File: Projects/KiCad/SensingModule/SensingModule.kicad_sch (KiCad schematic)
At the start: 37 parts, among them J3 Micro_SD_Card_Det_Hirose_DM3AT, J4 Conn_01x02_Pin, J5 Conn_01x05_Socket, J7 Conn_01x05_Pin, Q1 DTC143E, U1 NUCLEO-F303K8, U10 24LC1025, U11 MB85RS2MT, U12 TLP222A, U2 MCP2562-E-P, U3 24LC1025, U5 LT1584-3.3, U7 24LC1025, U8 MB85RS2MT, U9 24LC1025

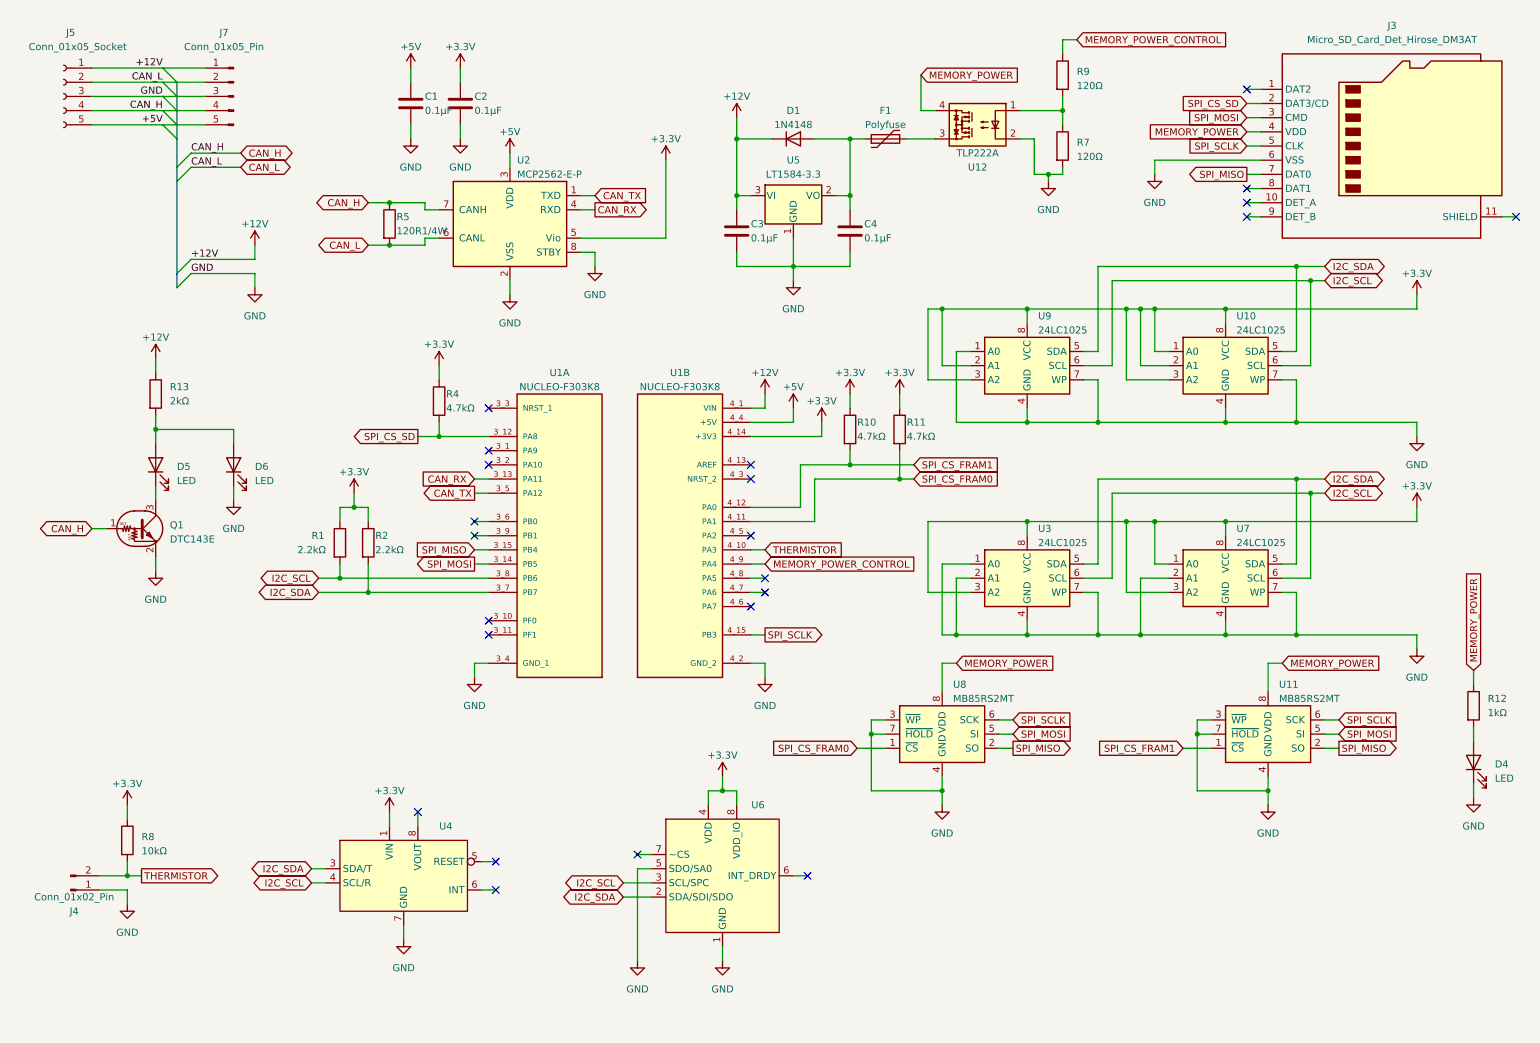
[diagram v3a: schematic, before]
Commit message: RCを解決
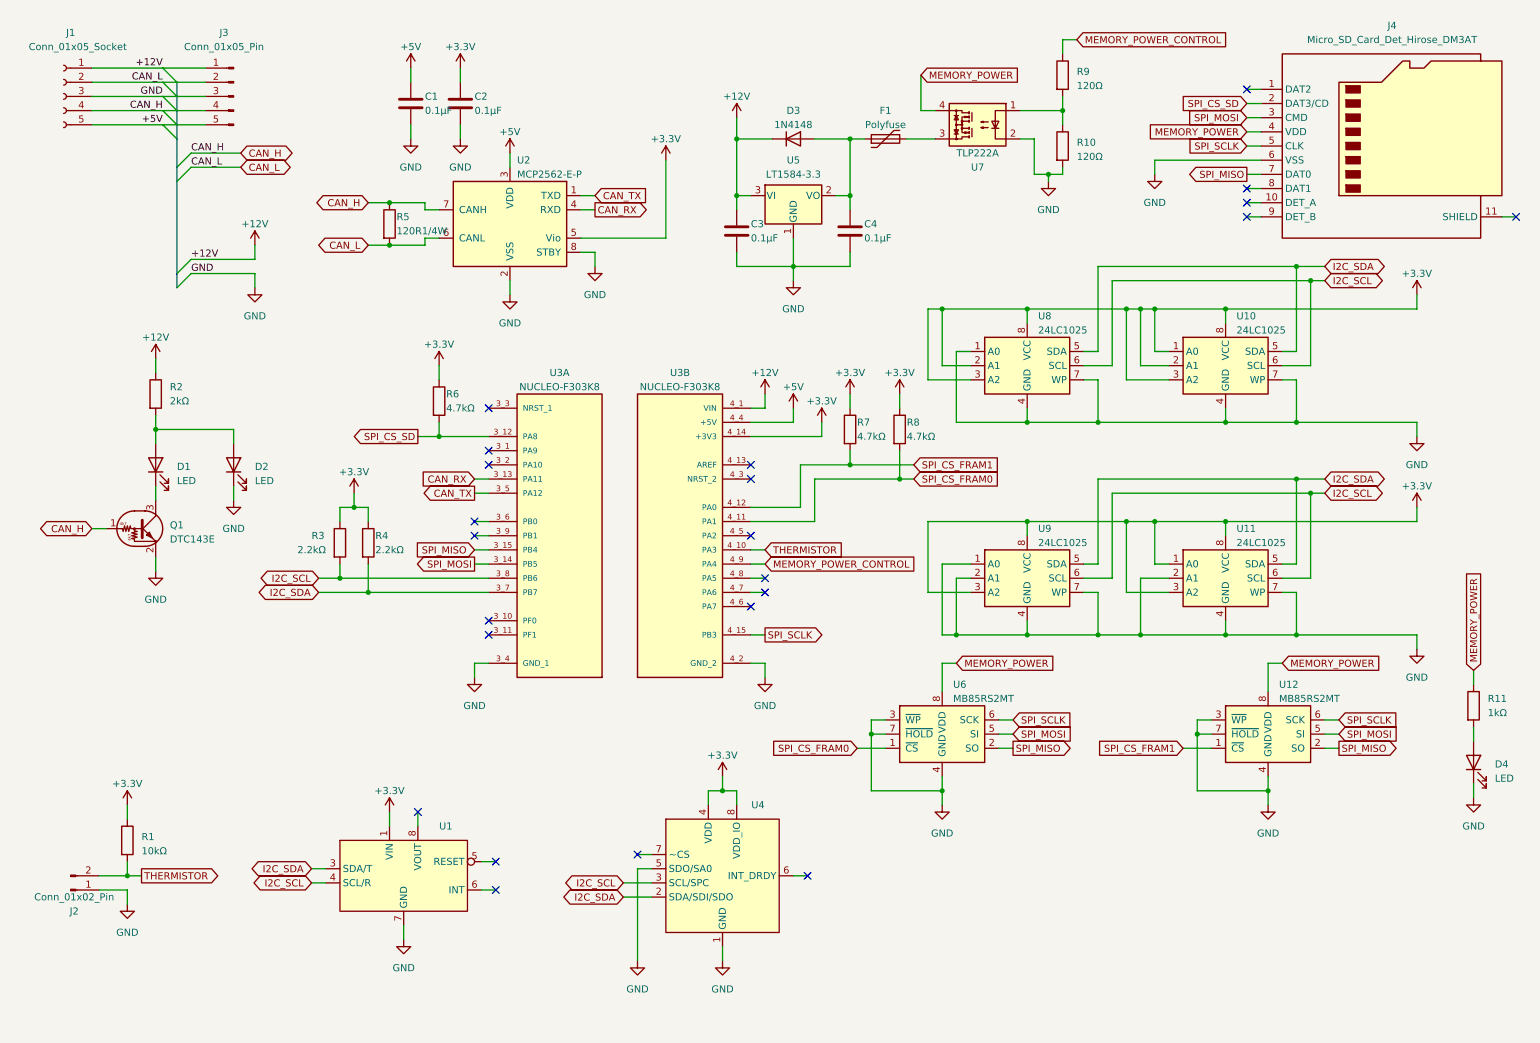
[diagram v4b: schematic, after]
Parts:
- renumbered D5 to D1, D6 to D2, D1 to D3, J5 to J1, J4 to J2, J7 to J3, J3 to J4, R8 to R1, R7 to R10, R12 to R11, R13 to R2, R1 to R3, R2 to R4, R4 to R6, R10 to R7, R11 to R8, U4 to U1, U7 to U11, U11 to U12, U1 to U3, U6 to U4, U8 to U6, U12 to U7, U9 to U8, U3 to U9

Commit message: 計測モジュールの基板設計概ね終わり
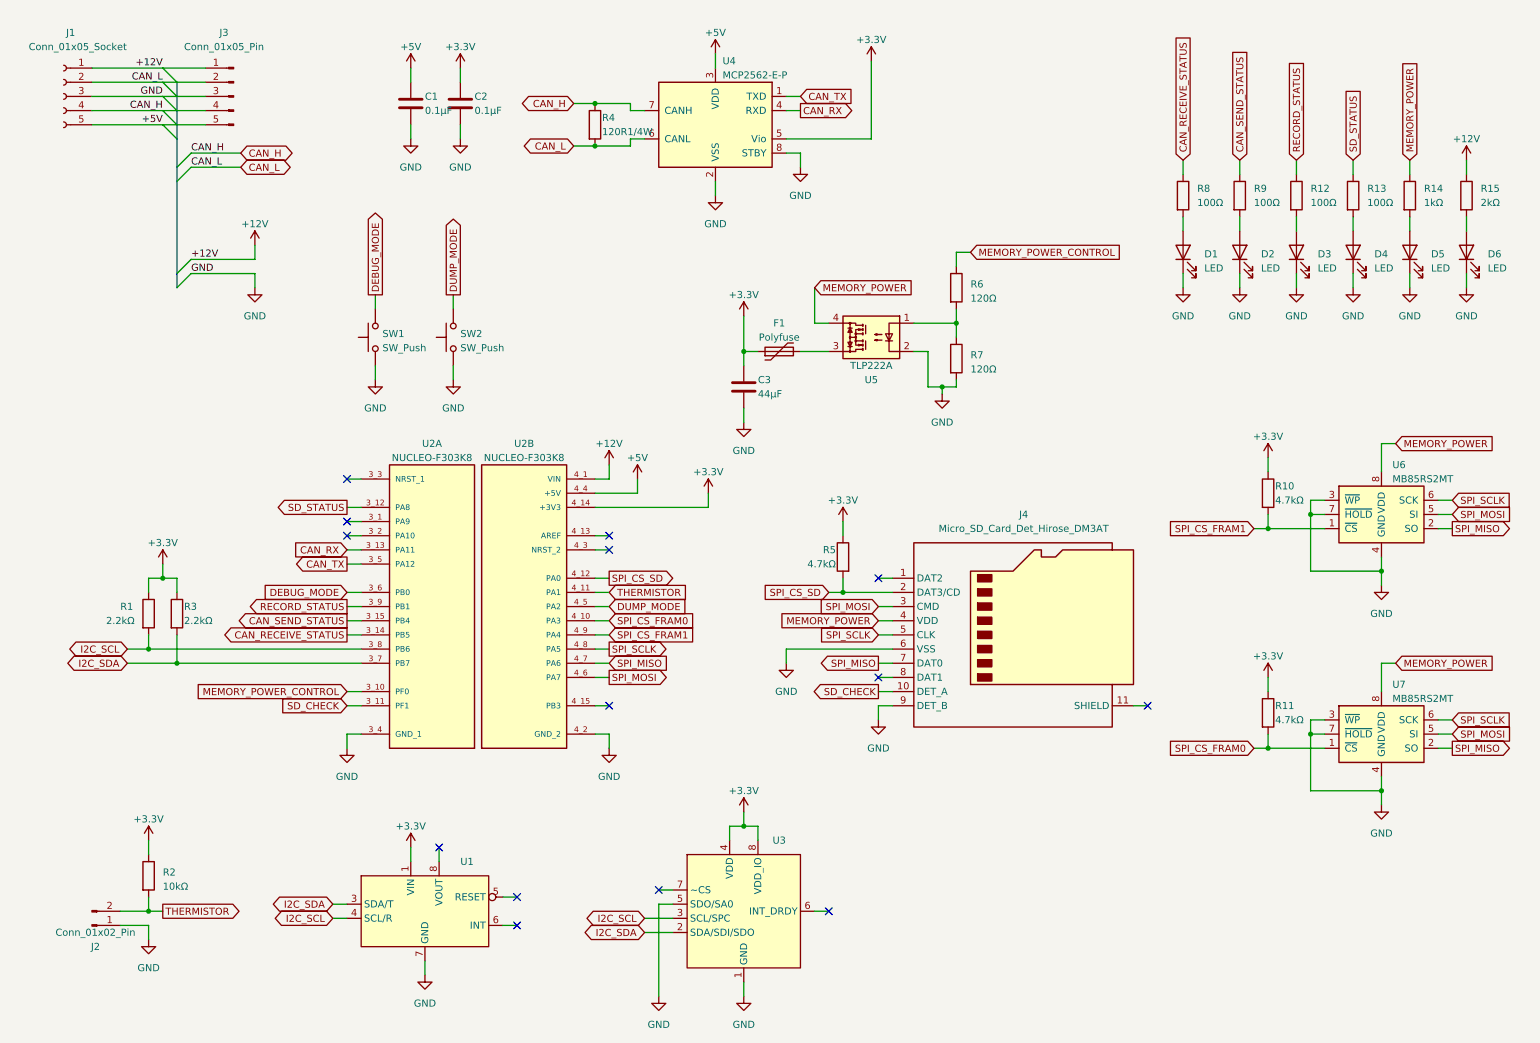
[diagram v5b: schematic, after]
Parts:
- removed C4: 0.1μF, Capacitor_SMD:C_0805_2012Metric_Pad1.18x1.45mm_HandSolder, symbol Device:C
- removed D3: 1N4148, Diode_THT:D_DO-35_SOD27_P7.62mm_Horizontal, symbol Diode:1N4148
- removed Q1: DTC143E, Package_TO_SOT_THT:TO-92_Inline, symbol Transistor_BJT:DTC143E
- removed U10, U11, U8, U9: 24LC1025, Package_DIP:DIP-8_W7.62mm, symbol Memory_EEPROM:24LC1025
- removed U5: LT1584-3.3, Package_TO_SOT_THT:TO-220-3_Vertical, symbol Regulator_Linear:LT1584-3.3
- added D2, D3, D4: LED, LED_SMD:LED_1206_3216Metric_Pad1.42x1.75mm_HandSolder, symbol Device:LED
- added R12, R13, R8, R9: 100Ω, Resistor_SMD:R_0805_2012Metric_Pad1.20x1.40mm_HandSolder, symbol Device:R
- added SW1, SW2: SW_Push, Button_Switch_THT:SW_PUSH_6mm, symbol Switch:SW_Push
- C3: value 0.1μF -> 44μF
- renumbered D4 to D5, D2 to D6, R3 to R1, R8 to R10, R7 to R11, R11 to R14, R2 to R15, R1 to R2, R4 to R3, R5 to R4, R6 to R5, R9 to R6, R10 to R7, U3 to U2, U4 to U3, U2 to U4, U7 to U5, U12 to U6, U6 to U7
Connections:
- net +12V: no longer C3.1
- net +3.3V: now also C3.1, F1.1
- net GND: now also D1.1 (K), J4.9 (DET_B), D2.1 (K), D3.1 (K), D4.1 (K), SW1.1, SW2.1
- net MEMORY_POWER_CONTROL: now also U2.3_10 (PF0); no longer U2.4_9 (PA4)
- net SPI_CS_FRAM0: now also R11.2, U2.4_10 (PA3); no longer R10.2, U2.4_11 (PA1)
- net SPI_CS_FRAM1: now also R10.2, U2.4_9 (PA4); no longer R11.2, U2.4_12 (PA0)
- net SPI_CS_SD: now also U2.4_12 (PA0); no longer U2.3_12 (PA8)
- net SPI_MISO: now also U2.4_7 (PA6); no longer U2.3_15 (PB4)
- net SPI_MOSI: now also U2.4_6 (PA7); no longer U2.3_14 (PB5)
- net SPI_SCLK: now also U2.4_8 (PA5); no longer U2.4_15 (PB3)
- net THERMISTOR: now also U2.4_11 (PA1); no longer U2.4_10 (PA3)
- net at D6.2 (A), R15.2: no longer D1.2 (A)
- net DUMP_MODE: now reaches U2.4_5 (PA2)
- net DUMP_MODE: now also SW2.2
- net SD_CHECK: now reaches J4.10 (DET_A)
- net SD_CHECK: now also U2.3_11 (PF1)
- net DEBUG_MODE: now reaches U2.3_6 (PB0)
- net DEBUG_MODE: now also SW1.2
- net RECORD_STATUS: now reaches U2.3_9 (PB1)
- net RECORD_STATUS: now also R12.1
- new net: D4.2 (A), R13.2
- new net: D2.2 (A), R9.2
- new net: D3.2 (A), R12.2
- new net: D1.2 (A), R8.2
- new net CAN_RECEIVE_STATUS: R8.1, U2.3_14 (PB5)
- new net CAN_SEND_STATUS: R9.1, U2.3_15 (PB4)
- new net SD_STATUS: R13.1, U2.3_12 (PA8)
- no-connect marks 23 -> 14
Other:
- moved on the sheet: D5, D6, F1, J2, J4, R1, R10, R11, R14, R15, R2, R3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

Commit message: 計測モジュールとフライトモジュール終わり
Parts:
- removed C3: 44μF, Capacitor_SMD:C_0805_2012Metric_Pad1.18x1.45mm_HandSolder, symbol Device:C
- removed U3: ~, StrawberryLinux_LPS33HW_Module:LPS33HW, symbol StrawberryLinux_LPS33HW_Module:LPS33HW
- added C3: 470μF, Capacitor_THT:CP_Radial_D10.0mm_P3.50mm, symbol Device:C_Polarized
- added U3: ~, Akizuki_BME280_Module:BME280, symbol Akizuki_BME280_Module:BME280
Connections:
- net +3.3V: now also C3.1, U3.1 (VDD), U3.3 (SCB)
- net GND: now also C3.2, U3.2 (GND), U3.5 (SDO)
- net I2C_SCL: now also U3.6 (SCK)
- net I2C_SDA: now also U3.4 (SDI)
- no-connect marks 14 -> 12

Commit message: アルミ殿下を導電性高分子アルミ固体電解コンデンサに変更
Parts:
- C3: value 470μF -> 100μF; footprint Capacitor_THT:CP_Radial_D10.0mm_P3.50mm -> Capacitor_SMD:CP_Elec_6.3x7.7
- R1, R3: value 2.2kΩ -> 10kΩ
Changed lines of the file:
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@@
       (effects (font (size 1.27 1.27)) (justify left))
     )
-    (property "Value" "2.2kΩ" (at 29.21 124.46 0)
+    (property "Value" "10kΩ" (at 29.21 124.46 0)
       (effects (font (size 1.27 1.27)) (justify left))
     )
@@
       (effects (font (size 1.27 1.27)) (justify left))
     )
-    (property "Value" "2.2kΩ" (at 43.18 124.46 0)
+    (property "Value" "10kΩ" (at 43.18 124.46 0)
       (effects (font (size 1.27 1.27)) (justify left))
     )
@@
       (effects (font (size 1.27 1.27)) (justify left))
     )
-    (property "Value" "470μF" (at 147.32 83.566 0)
-      (effects (font (size 1.27 1.27)) (justify left))
-    )
-    (property "Footprint" "Capacitor_THT:CP_Radial_D10.0mm_P3.50mm" (at 144.4752 86.36 0)
-      (effects (font (size 1.27 1.27)) hide)
-    )
+    (property "Value" "100μF" (at 147.32 83.566 0)
+      (effects (font (size 1.27 1.27)) (justify left))
+    )
+    (property "Footprint" "Capacitor_SMD:CP_Elec_6.3x7.7" (at 144.4752 86.36 0)
+      (effects (font (size 1.27 1.27)) hide)
+    )

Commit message: 抵抗とLEDを1608に変更
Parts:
- D1, D2, D3, D4, D5, D6: footprint LED_SMD:LED_1206_3216Metric_Pad1.42x1.75mm_HandSolder -> LED_SMD:LED_0603_1608Metric_Pad1.05x0.95mm_HandSolder
- R1, R10, R11, R12, R13, R14, R15, R2, R3, R4, R5, R6, R7, R8, R9: footprint Resistor_SMD:R_0805_2012Metric_Pad1.20x1.40mm_HandSolder -> Resistor_SMD:R_0603_1608Metric_Pad0.98x0.95mm_HandSolder
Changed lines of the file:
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@@
       (effects (font (size 1.27 1.27)) (justify left))
     )
-    (property "Footprint" "Resistor_SMD:R_0805_2012Metric_Pad1.20x1.40mm_HandSolder" (at 179.832 64.77 90)
+    (property "Footprint" "Resistor_SMD:R_0603_1608Metric_Pad0.98x0.95mm_HandSolder" (at 179.832 64.77 90)
       (effects (font (size 1.27 1.27)) hide)
     )
@@
       (effects (font (size 1.27 1.27)) (justify right))
     )
-    (property "Footprint" "LED_SMD:LED_1206_3216Metric_Pad1.42x1.75mm_HandSolder" (at 252.73 58.42 0)
+    (property "Footprint" "LED_SMD:LED_0603_1608Metric_Pad1.05x0.95mm_HandSolder" (at 252.73 58.42 0)
       (effects (font (size 1.27 1.27)) hide)
     )
@@
       (effects (font (size 1.27 1.27)) (justify left))
     )
-    (property "Footprint" "Resistor_SMD:R_0805_2012Metric_Pad1.20x1.40mm_HandSolder" (at 250.952 48.26 90)
+    (property "Footprint" "Resistor_SMD:R_0603_1608Metric_Pad0.98x0.95mm_HandSolder" (at 250.952 48.26 90)
       (effects (font (size 1.27 1.27)) hide)
     )
@@
       (effects (font (size 1.27 1.27)) (justify left))
     )
-    (property "Footprint" "Resistor_SMD:R_0805_2012Metric_Pad1.20x1.40mm_HandSolder" (at 230.632 48.26 90)
+    (property "Footprint" "Resistor_SMD:R_0603_1608Metric_Pad0.98x0.95mm_HandSolder" (at 230.632 48.26 90)
       (effects (font (size 1.27 1.27)) hide)
     )
@@
       (effects (font (size 1.27 1.27)) (justify left))
     )
-    (property "Footprint" "Resistor_SMD:R_0805_2012Metric_Pad1.20x1.40mm_HandSolder" (at 271.272 48.26 90)
+    (property "Footprint" "Resistor_SMD:R_0603_1608Metric_Pad0.98x0.95mm_HandSolder" (at 271.272 48.26 90)
       (effects (font (size 1.27 1.27)) hide)
     )
@@
       (effects (font (size 1.27 1.27)) (justify left))
     )
-    (property "Footprint" "Resistor_SMD:R_0805_2012Metric_Pad1.20x1.40mm_HandSolder" (at 35.052 170.18 90)
+    (property "Footprint" "Resistor_SMD:R_0603_1608Metric_Pad0.98x0.95mm_HandSolder" (at 35.052 170.18 90)
       (effects (font (size 1.27 1.27)) hide)
     )
@@
       (effects (font (size 1.27 1.27)) (justify right))
     )
-    (property "Footprint" "LED_SMD:LED_1206_3216Metric_Pad1.42x1.75mm_HandSolder" (at 242.57 58.42 0)
+    (property "Footprint" "LED_SMD:LED_0603_1608Metric_Pad1.05x0.95mm_HandSolder" (at 242.57 58.42 0)
       (effects (font (size 1.27 1.27)) hide)
     )
@@
       (effects (font (size 1.27 1.27)) (justify left))
     )
-    (property "Footprint" "Resistor_SMD:R_0805_2012Metric_Pad1.20x1.40mm_HandSolder" (at 163.068 113.03 90)
+    (property "Footprint" "Resistor_SMD:R_0603_1608Metric_Pad0.98x0.95mm_HandSolder" (at 163.068 113.03 90)
       (effects (font (size 1.27 1.27)) hide)
     )
@@
       (effects (font (size 1.27 1.27)) (justify left))
     )
-    (property "Footprint" "Resistor_SMD:R_0805_2012Metric_Pad1.20x1.40mm_HandSolder" (at 240.792 48.26 90)
+    (property "Footprint" "Resistor_SMD:R_0603_1608Metric_Pad0.98x0.95mm_HandSolder" (at 240.792 48.26 90)
       (effects (font (size 1.27 1.27)) hide)
     )
@@
       (effects (font (size 1.27 1.27)) (justify left))
     )
-    (property "Footprint" "Resistor_SMD:R_0805_2012Metric_Pad1.20x1.40mm_HandSolder" (at 261.112 48.26 90)
+    (property "Footprint" "Resistor_SMD:R_0603_1608Metric_Pad0.98x0.95mm_HandSolder" (at 261.112 48.26 90)
       (effects (font (size 1.27 1.27)) hide)
     )
@@
       (effects (font (size 1.27 1.27)) (justify left))
     )
-    (property "Footprint" "Resistor_SMD:R_0805_2012Metric_Pad1.20x1.40mm_HandSolder" (at 235.712 140.97 90)
+    (property "Footprint" "Resistor_SMD:R_0603_1608Metric_Pad0.98x0.95mm_HandSolder" (at 235.712 140.97 90)
       (effects (font (size 1.27 1.27)) hide)
     )
@@
       (effects (font (size 1.27 1.27)) (justify left))
     )
-    (property "Footprint" "Resistor_SMD:R_0805_2012Metric_Pad1.20x1.40mm_HandSolder" (at 35.052 123.19 90)
+    (property "Footprint" "Resistor_SMD:R_0603_1608Metric_Pad0.98x0.95mm_HandSolder" (at 35.052 123.19 90)
       (effects (font (size 1.27 1.27)) hide)
     )
@@
       (effects (font (size 1.27 1.27)) (justify right))
     )
-    (property "Footprint" "LED_SMD:LED_1206_3216Metric_Pad1.42x1.75mm_HandSolder" (at 273.05 58.42 0)
+    (property "Footprint" "LED_SMD:LED_0603_1608Metric_Pad1.05x0.95mm_HandSolder" (at 273.05 58.42 0)
       (effects (font (size 1.27 1.27)) hide)
     )
@@
       (effects (font (size 1.27 1.27)) (justify right))
     )
-    (property "Footprint" "LED_SMD:LED_1206_3216Metric_Pad1.42x1.75mm_HandSolder" (at 222.25 58.42 0)
+    (property "Footprint" "LED_SMD:LED_0603_1608Metric_Pad1.05x0.95mm_HandSolder" (at 222.25 58.42 0)
       (effects (font (size 1.27 1.27)) hide)
     )
@@
       (effects (font (size 1.27 1.27)) (justify left))
     )
-    (property "Footprint" "Resistor_SMD:R_0805_2012Metric_Pad1.20x1.40mm_HandSolder" (at 179.832 77.47 90)
+    (property "Footprint" "Resistor_SMD:R_0603_1608Metric_Pad0.98x0.95mm_HandSolder" (at 179.832 77.47 90)
       (effects (font (size 1.27 1.27)) hide)
     )
@@
       (effects (font (size 1.27 1.27)) (justify left))
     )
-    (property "Footprint" "Resistor_SMD:R_0805_2012Metric_Pad1.20x1.40mm_HandSolder" (at 235.712 101.6 90)
+    (property "Footprint" "Resistor_SMD:R_0603_1608Metric_Pad0.98x0.95mm_HandSolder" (at 235.712 101.6 90)
       (effects (font (size 1.27 1.27)) hide)
     )
@@
       (effects (font (size 1.27 1.27)) (justify right))
     )
-    (property "Footprint" "LED_SMD:LED_1206_3216Metric_Pad1.42x1.75mm_HandSolder" (at 232.41 58.42 0)
+    (property "Footprint" "LED_SMD:LED_0603_1608Metric_Pad1.05x0.95mm_HandSolder" (at 232.41 58.42 0)
       (effects (font (size 1.27 1.27)) hide)
     )
@@
       (effects (font (size 1.27 1.27)) (justify left))
     )
-    (property "Footprint" "Resistor_SMD:R_0805_2012Metric_Pad1.20x1.40mm_HandSolder" (at 40.132 123.19 90)
+    (property "Footprint" "Resistor_SMD:R_0603_1608Metric_Pad0.98x0.95mm_HandSolder" (at 40.132 123.19 90)
       (effects (font (size 1.27 1.27)) hide)
     )
@@
       (effects (font (size 1.27 1.27)) (justify right))
     )
-    (property "Footprint" "LED_SMD:LED_1206_3216Metric_Pad1.42x1.75mm_HandSolder" (at 262.89 58.42 0)
+    (property "Footprint" "LED_SMD:LED_0603_1608Metric_Pad1.05x0.95mm_HandSolder" (at 262.89 58.42 0)
       (effects (font (size 1.27 1.27)) hide)
     )
@@
       (effects (font (size 1.27 1.27)) (justify left))
     )
-    (property "Footprint" "Resistor_SMD:R_0805_2012Metric_Pad1.20x1.40mm_HandSolder" (at 220.472 48.26 90)
+    (property "Footprint" "Resistor_SMD:R_0603_1608Metric_Pad0.98x0.95mm_HandSolder" (at 220.472 48.26 90)
       (effects (font (size 1.27 1.27)) hide)
     )
@@
       (effects (font (size 1.27 1.27)) (justify left))
     )
-    (property "Footprint" "Resistor_SMD:R_0805_2012Metric_Pad1.20x1.40mm_HandSolder" (at 115.062 35.56 90)
-      (effects (font (size 1.27 1.27)) hide)
-    )
+    (property "Footprint" "Resistor_SMD:R_0603_1608Metric_Pad0.98x0.95mm_HandSolder" (at 115.062 35.56 90)
+      (effects (font (size 1.27 1.27)) hide)
+    )
